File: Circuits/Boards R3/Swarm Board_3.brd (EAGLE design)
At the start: 82.1 x 63.5 mm, 139 parts, among them CON1 ISP(2X3), CON2 MAIN_CONNECTOR_14SMD, CON4 HEADER_3X1, CON5 HEADER_3X1, CON7 MAIN_CONNECTOR_8, M1 VIBMOTOR, T1 TEFT4300, T10 TEFT4300, T11 NPN2N2222, T12 SI2333DS-T1, T13 NPN2N2222, T14 NPN2N2222, T15 NPN2N2222, T16 NPN2N2222, T17 NPN2N2222, T18 NPN2N2222, T19 IRLML6244TR, T2 TEFT4300, T20 IRLML6244TR, T21 IRLML6244TR, T22 IRLML6244TR, T23 IRLML6244TR, T3 NPN2N2222, T4 TEFT4300, T5 TEFT4300, T6 TEFT4300, T7 TEFT4300, T8 TEFT4300, T9 TEFT4300, U1 ATMEGA324P, U2 MCP73833, U3 ATMEGA1281, U4 MCP9700A, U5 AH182, U6 AH182, U7 QRE1113, U8 QRE1113, U9 QRE1113

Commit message: MORE STUFF
LEDS, TX/RX, WHATEVER
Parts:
- LED11, LED12: value (none) -> RED
- LED14, LED15: value (none) -> GREEN
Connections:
- new net LED5: R56.1
- net LED4: no longer R53.1, R55.1, R56.1
- net MISO: now also R55.1
- net MOSI: now also R53.1
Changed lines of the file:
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@@
 <element name="U9" library="Passive" package="QRE1113" value="QRE1113" x="93.853" y="33.909"/>
 <element name="R52" library="Passive" package="0603" value="100" x="88.646" y="18.415"/>
-<element name="LED11" library="Passive" package="LED0603" value="" x="-64.262" y="-67.945"/>
+<element name="LED11" library="Passive" package="LED0603" value="RED" x="-64.262" y="-67.945"/>
 <element name="R53" library="Passive" package="0603" value="1k" x="-67.183" y="-67.945"/>
-<element name="LED12" library="Passive" package="LED0603" value="" x="-67.183" y="-74.549"/>
+<element name="LED12" library="Passive" package="LED0603" value="RED" x="-67.183" y="-74.549"/>
 <element name="R54" library="Passive" package="0603" value="1k" x="-67.183" y="-71.247"/>
-<element name="LED14" library="Passive" package="LED0603" value="" x="-67.183" y="-80.391"/>
+<element name="LED14" library="Passive" package="LED0603" value="GREEN" x="-67.183" y="-80.391"/>
 <element name="R55" library="Passive" package="0603" value="1k" x="-67.183" y="-77.089"/>
-<element name="LED15" library="Passive" package="LED0603" value="" x="-67.183" y="-86.233"/>
+<element name="LED15" library="Passive" package="LED0603" value="GREEN" x="-67.183" y="-86.233"/>
 <element name="R56" library="Passive" package="0603" value="1k" x="-67.183" y="-82.931"/>
 <element name="C7" library="Passive" package="0603" value="1uf" x="23.495" y="60.1345" rot="R180"/>
@@
 <contactref element="CON1" pad="6"/>
 <contactref element="U3" pad="P$13"/>
-<wire x1="-1.146" y1="-16.554" x2="72.39" y2="13.081" width="0" layer="19" extent="1-1"/>
+<contactref element="R55" pad="1"/>
+<wire x1="-1.146" y1="-16.554" x2="-67.933" y2="-77.089" width="0" layer="19" extent="1-1"/>
+<wire x1="72.39" y1="13.081" x2="-1.146" y2="-16.554" width="0" layer="19" extent="1-1"/>
 </signal>
 <signal name="TEMPSENSE">
@@
 <contactref element="CON1" pad="2"/>
 <contactref element="U3" pad="P$12"/>
-<wire x1="-1.146" y1="-15.754" x2="69.85" y2="15.621" width="0" layer="19" extent="1-1"/>
+<contactref element="R53" pad="1"/>
+<wire x1="-1.146" y1="-15.754" x2="-67.933" y2="-67.945" width="0" layer="19" extent="1-1"/>
+<wire x1="69.85" y1="15.621" x2="-1.146" y2="-15.754" width="0" layer="19" extent="1-1"/>
 </signal>
 <signal name="SCK">
@@
 </signal>
 <signal name="LED4">
-<contactref element="R53" pad="1"/>
 <contactref element="R54" pad="1"/>
-<contactref element="R55" pad="1"/>
-<contactref element="R56" pad="1"/>
-<wire x1="-67.933" y1="-77.089" x2="-67.933" y2="-82.931" width="0" layer="19" extent="1-1"/>
-<wire x1="-67.933" y1="-71.247" x2="-67.933" y2="-77.089" width="0" layer="19" extent="1-1"/>
-<wire x1="-67.933" y1="-67.945" x2="-67.933" y2="-71.247" width="0" layer="19" extent="1-1"/>
 </signal>
 <signal name="N$45">
@@
 <wire x1="-71.3265" y1="-92.9165" x2="-66.433" y2="-106.68" width="0" layer="19" extent="1-1"/>
 </signal>
+<signal name="LED5">
+<contactref element="R56" pad="1"/>
+</signal>
 </signals>

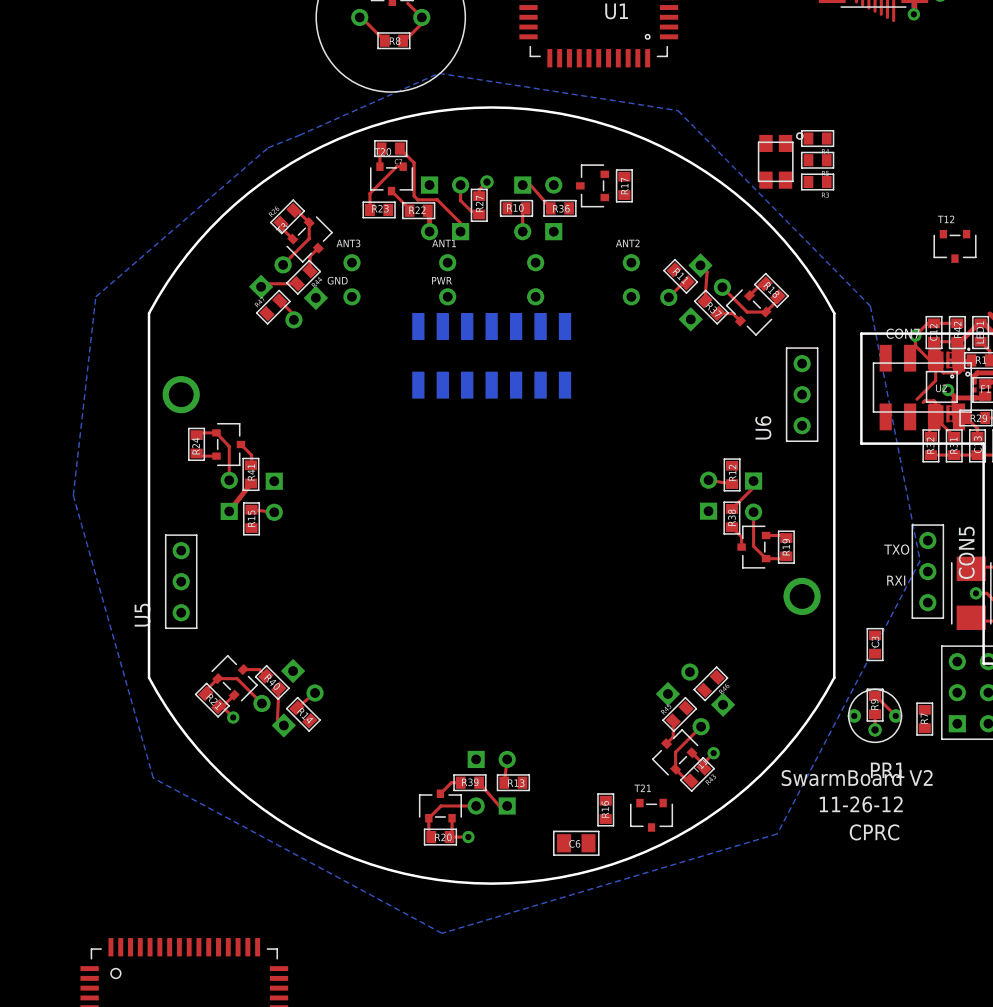
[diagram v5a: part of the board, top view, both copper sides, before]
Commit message: Both boards almost ready for routing
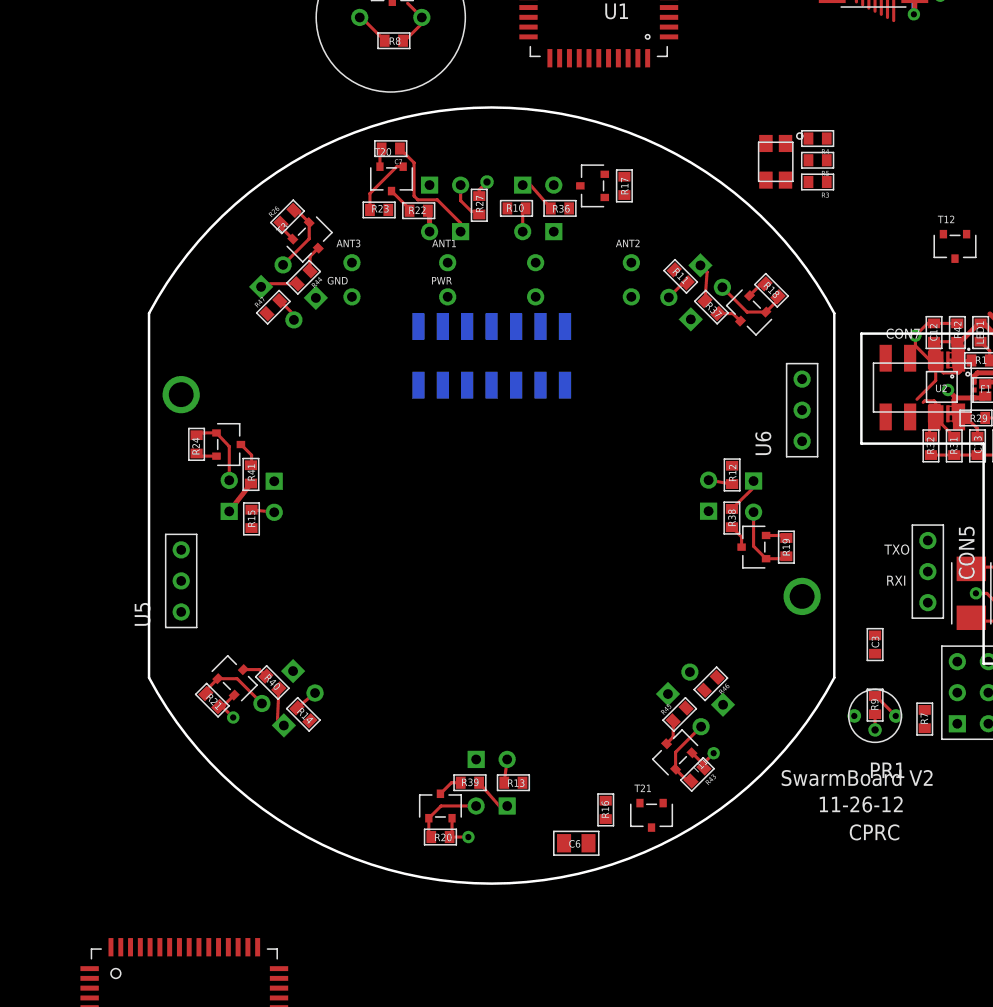
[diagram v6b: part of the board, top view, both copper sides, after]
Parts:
- moved U6 1.27 mm to (57.1, 38.7)
- moved U5 0.06 mm to (6.35, 24.8)
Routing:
- added copper zone on layer 15, net +3V
- added copper zone on layer 15, net +VSENSE
- added copper zone on layer 2, net GND
- removed copper zone on layer 16, net GND

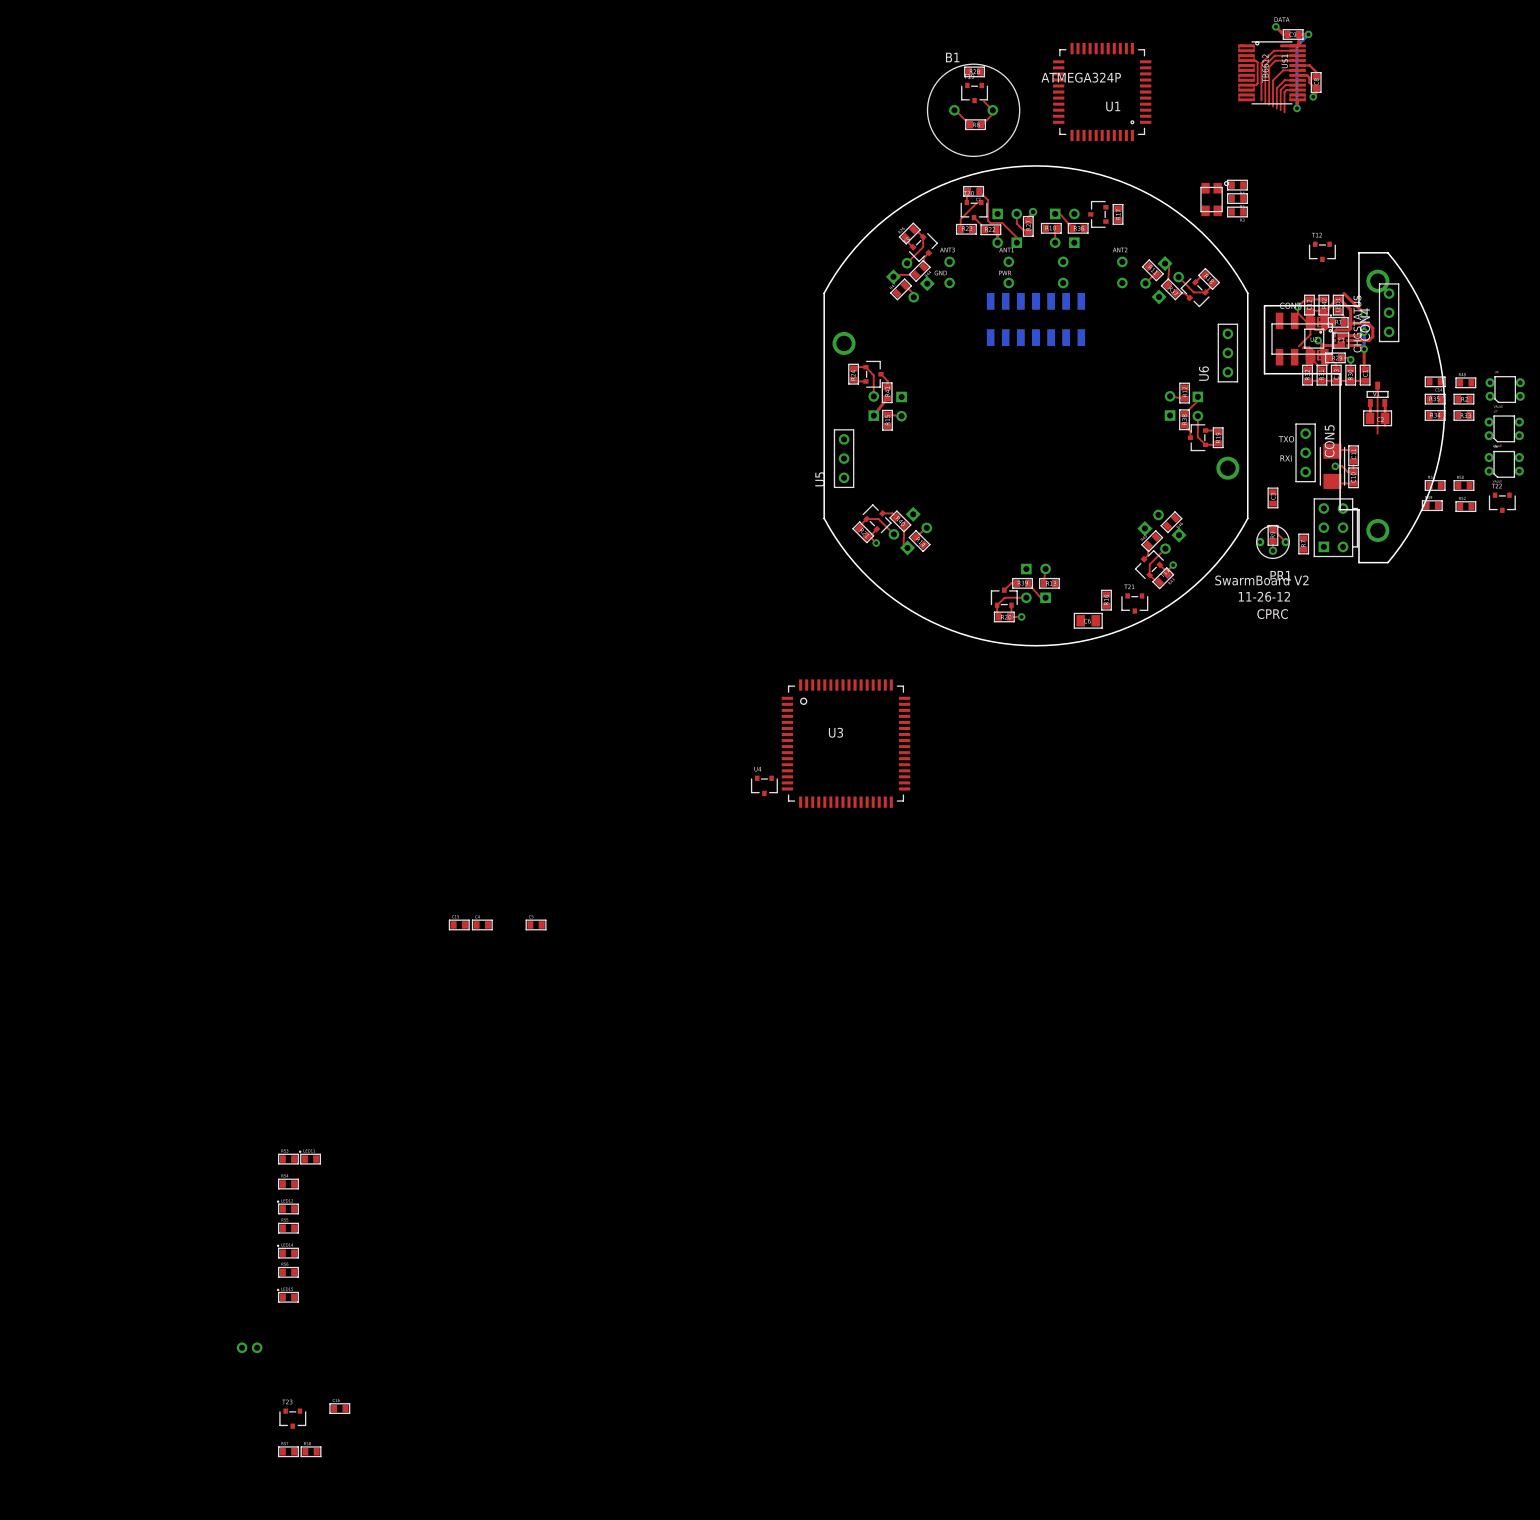
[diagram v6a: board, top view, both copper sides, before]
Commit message: picked new 3v regulator
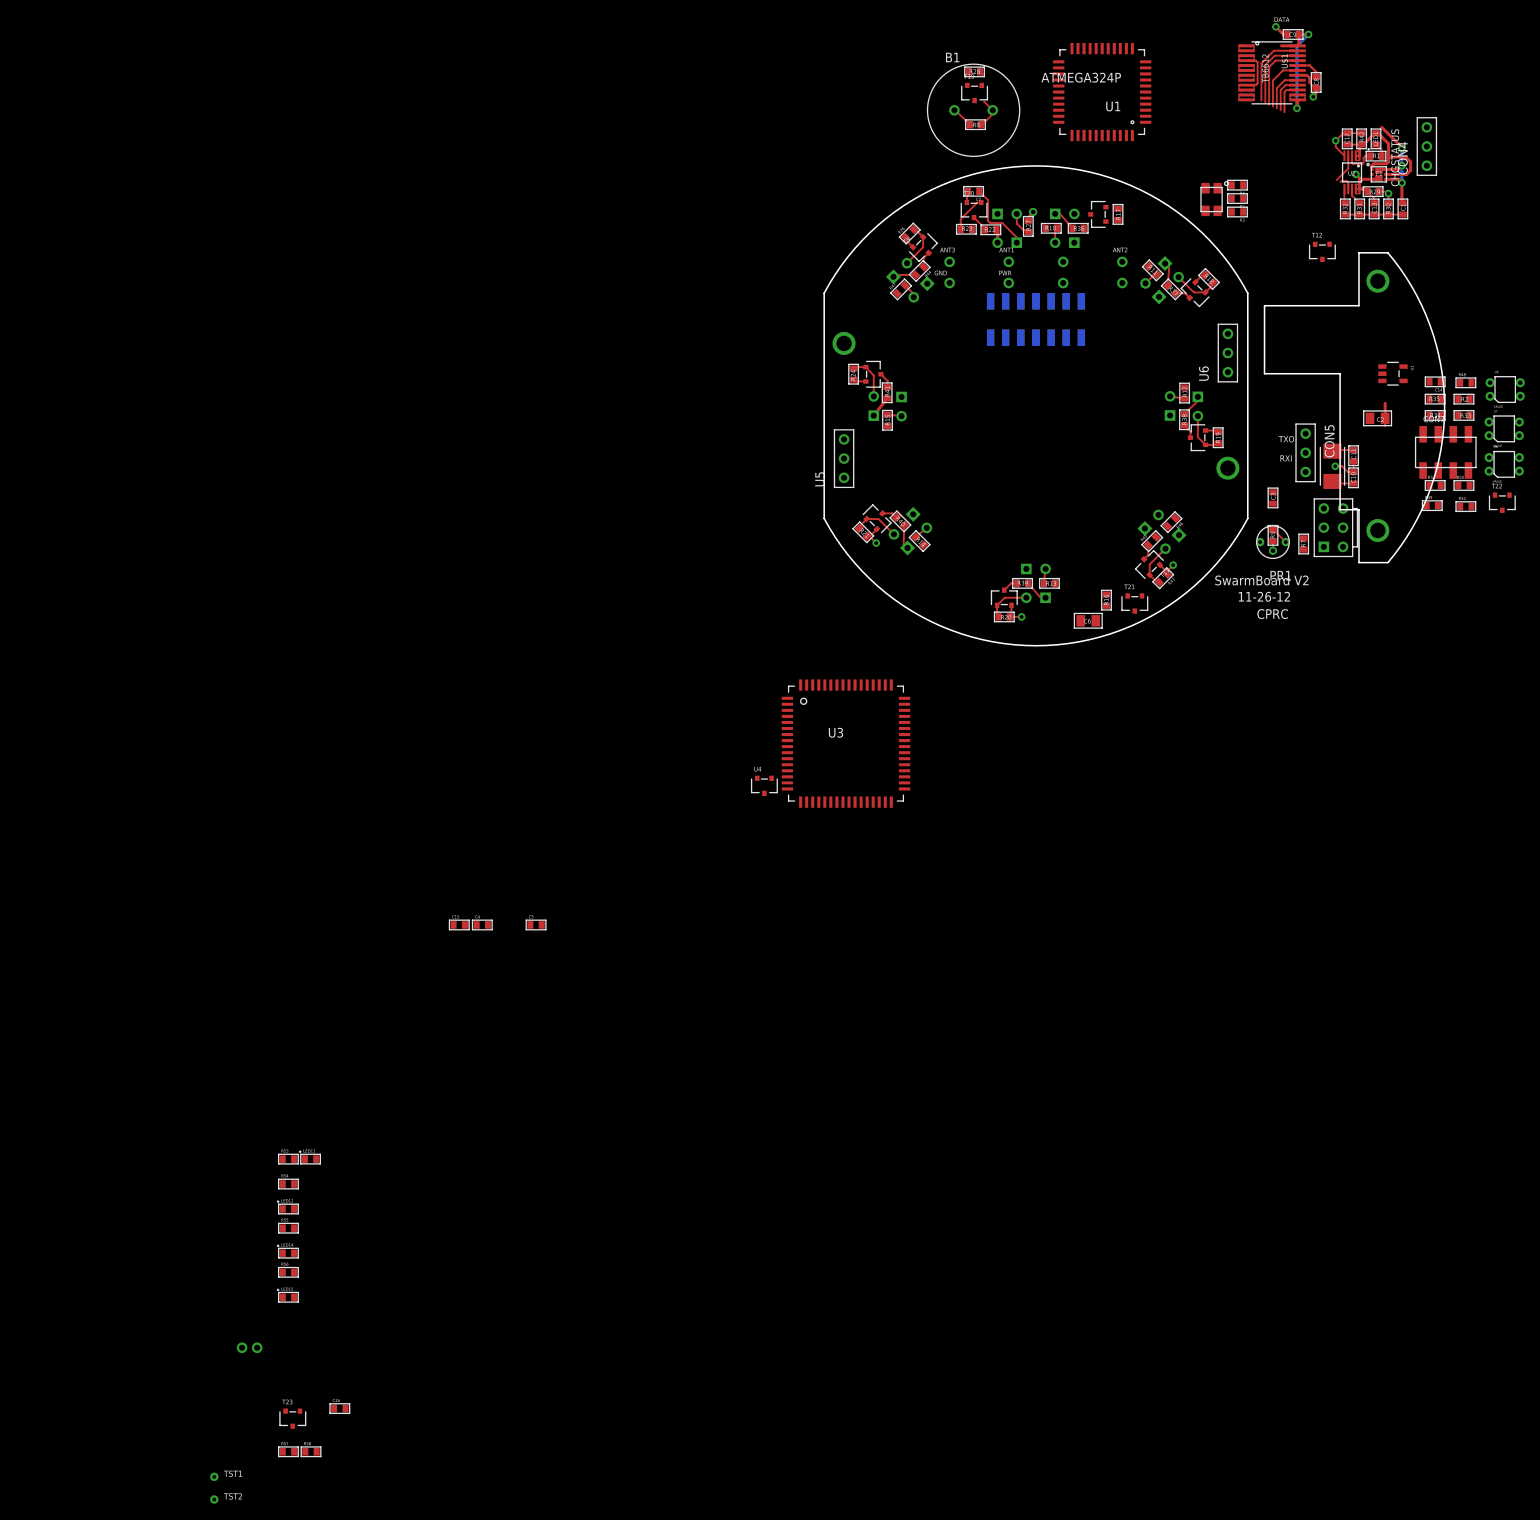
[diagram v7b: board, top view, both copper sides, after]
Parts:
- added TST1, TST2: TESTPOINT, Mechanical:TESTPOINT
- V1: value MCP1700-3002E -> XC6210B302; device PowerIC:(TT/NB)SOT-23(3PAD) -> PowerIC:(OT)SOT-23(5PAD)
- moved CON7 24.2 mm to (86.0, 25.6)
- moved R1 22.6 mm to (76.8, 64.8)
- moved C1 22.6 mm to (80.3, 57.8)
- moved C13 22.6 mm to (76.5, 57.8)
- moved CON4 22.6 mm to (83.5, 66.1)
- moved F1 22.6 mm to (77.1, 62.4)
- moved R29 22.6 mm to (76.4, 60.1)
- moved R30 22.6 mm to (78.4, 57.8)
- moved R31 22.6 mm to (74.6, 57.8)
- moved R32 22.6 mm to (72.7, 57.8)
- moved U2 22.6 mm to (73.6, 62.6)
- moved C12 22.6 mm to (72.9, 67.1)
- moved LED1 22.6 mm to (76.8, 67.1)
- moved R42 22.6 mm to (74.8, 67.1)
- moved V1 3.40 mm to (79.0, 36.0), turned to 270 degrees
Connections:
- removed net SCL: ANT4.P$1, ANT4.P$2, U3.P$25
- removed net SDA: ANT2.P$1, ANT2.P$2, U3.P$26
- new net CRX: ANT4.P$1, ANT4.P$2, U3.P$2
- new net CTX: ANT2.P$1, ANT2.P$2, U3.P$3
- new net DEBUG1: TST1.P$1
- new net DEBUG2: TST2.P$1
- new net VIBE: R58.1
- net +3V: now also C16.1, C9.1, M1.P$1, U$1.13, U$1.14, U$1.24, V1.5; no longer V1.2
- net +VRAW: now also V1.1; no longer C16.1, C9.1, M1.P$1, U$1.13, U$1.14, U$1.24
- net DATAANTENNA: now also U3.P$28; no longer U1.10
- net DISTANCELED: no longer R58.1
- net GND: now also V1.2; no longer V1.1
- net N$8: now also U3.P$27; no longer U1.9
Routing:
- net +VRAW: track 39.7 -> 16.8 mm, vias 5 -> 3
- net +3V: track 19.6 -> 36.0 mm, vias 0 -> 2
- net GND: track 53.3 -> 51.3 mm

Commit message: ready to route
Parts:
- removed U9: QRE1113, Passive:QRE1113
- added C17: 10uf, Passive:CAP-PTH-SMALL-POL
- added R25, R59, R6, R60, R61, R62: 10k, Passive:0603
- C2: value 10uf -> 1uf; device Passive:0805 -> Passive:0603
- C3, C8: value 1uf -> .1uf
- R34: value 22k -> 10k
- R52: value 100 -> 10k
- moved R34 223.7 mm to (-87.0, -113.0)
- moved R52 221.8 mm to (-90.0, -113.0)
- moved C2 0.11 mm to (77.0, 30.0), turned to 0 degrees
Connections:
- net IRBUMBER renamed ????
- removed net SIRBUMPER: CON7.5, R34.2, U9.P$4
- new net LED6: R55.1
- new net LED7: R56.1
- new net N$49: R25.2
- new net N$50: R34.2
- new net N$51: R52.2
- new net N$52: R59.2
- new net N$53: R60.2
- new net N$54: R61.2
- new net N$55: R62.2
- new net N$56: U3.P$25
- new net N$57: U3.P$26
- new net N$58: U3.P$8
- new net N$59: U3.P$9
- new net PB0: U3.P$10
- new net PB4: U3.P$14
- new net PB5: U3.P$15
- new net PB6: U3.P$16
- new net PB7: U3.P$17
- new net S????: CON7.5
- net +3V: now also C17.+
- net APWM: now also U3.P$5
- net BPWM: now also U3.P$6
- net BUZZER: now also U3.P$1
- net GND: now also C17.-
- net LED4: now also R53.1, U3.P$7; no longer R54.1
- net LED5: now also R54.1; no longer R56.1
- net MISO: no longer R55.1
- net MOSI: no longer R53.1
- net N$2: no longer R52.2
- net N$42: now also R6.2; no longer R52.1, U9.P$2
- net RX1: now also R6.1
- net RX2: now also R25.1
- net RX3: now also R34.1
- net RX4: now also R52.1
- net RX5: now also R59.1
- net RX6: now also R60.1
- net RX7: now also R61.1
- net RX8: now also R62.1
- net S+VSENSE: no longer U9.P$1, U9.P$3
- net SGND: no longer R34.1
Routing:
- net +3V: track 36.0 -> 33.1 mm
